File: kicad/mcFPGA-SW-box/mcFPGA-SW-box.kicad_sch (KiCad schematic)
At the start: 120 parts, among them J1 Conn_01x04, J10 Conn_01x02, J11 Conn_01x02, J12 Conn_01x02, J2 Conn_01x04, J4 Conn_01x04, J5 Conn_01x04, J6 Conn_01x04, J8 Conn_01x02, U1 74HC595, U10 NC7SB3157P6X, U11 NC7SB3157P6X, U12 NC7SB3157P6X, U13 NC7SB3157P6X, U14 NC7SB3157P6X, U15 NC7SB3157P6X, U16 NC7SB3157P6X, U17 NC7SB3157P6X, U18 NC7SB3157P6X, U19 NC7SB3157P6X, U2 74HC595, U20 NC7SB3157P6X, U21 NC7SB3157P6X, U22 NC7SB3157P6X, U23 NC7SB3157P6X, U24 NC7SB3157P6X, U25 NC7SB3157P6X, U26 NC7SB3157P6X, U27 NC7SB3157P6X, U28 NC7SB3157P6X, U29 NC7SB3157P6X, U3 74HC595, U30 NC7SB3157P6X, U31 NC7SB3157P6X, U32 NC7SB3157P6X, U33 NC7SB3157P6X, U34 NC7SB3157P6X, U35 NC7SB3157P6X, U36 NC7SB3157P6X, U4 74HC595, U5 NC7SB3157P6X, U6 NC7SB3157P6X, U7 NC7SB3157P6X, U8 NC7SB3157P6X, U9 NC7SB3157P6X

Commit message: start layout of SW box
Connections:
- net GND: now also J1.4 (Pin_4); no longer J1.1 (Pin_1)
- net LATCH: now also J1.3 (Pin_3); no longer J1.2 (Pin_2)
- net MOSI: now also J1.2 (Pin_2); no longer J1.3 (Pin_3)
- net SCLK: now also J1.1 (Pin_1); no longer J1.4 (Pin_4)
- net prio_east_0: no longer J12.2 (Pin_2)
- net prio_west_0: now also U26.1; no longer U26.4
- net prio_west_1: now also U25.1; no longer U25.4
- net west_0: now also U8.3; no longer U8.4
- net west_1: now also U7.3; no longer U7.4
- net west_2: now also U6.3; no longer U6.4
- net west_3: now also U5.3; no longer U5.4
- net at U29.4, U33.4, U36.4: now also U26.4; no longer U26.1
- net at U12.4, U22.4: now also U6.4; no longer U6.1
- net at U28.4, U32.4, U35.4: now also U25.4; no longer U25.1
- net at U18.4, U24.4: now also U8.4; no longer U8.1
- net at U21.4, U9.4: now also U5.4; no longer U5.1
- net at U15.4, U23.4: now also U7.4; no longer U7.1
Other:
- moved on the sheet: J1, J10, J11, J12, J2, J8, U25A, U26A, U27A, U28A, U29A, U30A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

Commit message: SWbox layout nearly complete
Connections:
- net prio_east_0: now also J12.2 (Pin_2)
- net west_0: now also U8.1; no longer U8.3
- net west_1: now also U7.1; no longer U7.3
- net west_2: now also U6.1; no longer U6.3
- net west_3: now also U5.1; no longer U5.3
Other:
- moved on the sheet: J12, J?
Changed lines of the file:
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@@
   (junction (at 158.115 227.965) (diameter 0) (color 0 0 0 0)
   )
+  (no_connect (at 105.41 119.38))
   (no_connect (at 297.18 60.96))
   (no_connect (at 162.56 144.78))
-  (no_connect (at 105.41 106.68))
   (no_connect (at 374.65 60.96))
   (no_connect (at 223.52 109.22))
-  (no_connect (at 105.41 124.46))
   (no_connect (at 142.24 144.78))
-  (no_connect (at 105.41 88.9))
   (no_connect (at 201.93 119.38))
   (no_connect (at 162.56 40.64))
+  (no_connect (at 105.41 66.04))
   (no_connect (at 182.88 40.64))
   (no_connect (at 331.47 116.84))
+  (no_connect (at 105.41 101.6))
   (no_connect (at 182.88 144.78))
   (no_connect (at 331.47 39.37))
@@
   (no_connect (at 161.29 83.82))
   (no_connect (at 351.79 39.37))
-  (no_connect (at 105.41 71.12))
   (no_connect (at 331.47 71.12))
   (no_connect (at 181.61 101.6))
@@
   (no_connect (at 140.97 66.04))
   (no_connect (at 203.2 40.64))
+  (no_connect (at 105.41 83.82))
   (no_connect (at 223.52 73.66))
   (no_connect (at 142.24 40.64))
@@
     (stroke (width 0) (type default))
   )
-  (wire (pts (xy 388.62 68.58) (xy 377.19 68.58))
+  (wire (pts (xy 377.19 68.58) (xy 389.89 68.58))
     (stroke (width 0) (type default))
   )
@@
     (stroke (width 0) (type default))
   )
-  (wire (pts (xy 88.9 88.9) (xy 99.06 88.9))
+  (wire (pts (xy 88.9 93.98) (xy 99.06 93.98))
     (stroke (width 0) (type default))
   )
@@
     (stroke (width 0) (type default))
   )
-  (wire (pts (xy 105.41 83.82) (xy 101.6 83.82))
+  (wire (pts (xy 105.41 88.9) (xy 101.6 88.9))
     (stroke (width 0) (type default))
   )
@@
     (stroke (width 0) (type default))
   )
-  (wire (pts (xy 88.9 96.52) (xy 99.06 96.52))
+  (wire (pts (xy 88.9 101.6) (xy 99.06 101.6))
     (stroke (width 0) (type default))
   )
@@
     (stroke (width 0) (type default))
   )
-  (wire (pts (xy 101.6 83.82) (xy 101.6 91.44))
+  (wire (pts (xy 101.6 88.9) (xy 101.6 96.52))
     (stroke (width 0) (type default))
   )
@@
     (stroke (width 0) (type default))
   )
-  (wire (pts (xy 88.9 93.98) (xy 101.6 93.98))
+  (wire (pts (xy 88.9 99.06) (xy 101.6 99.06))
     (stroke (width 0) (type default))
   )
@@
     (stroke (width 0) (type default))
   )
-  (wire (pts (xy 374.65 66.04) (xy 389.255 66.04))
+  (wire (pts (xy 374.65 66.04) (xy 389.89 66.04))
     (stroke (width 0) (type default))
   )
@@
     (stroke (width 0) (type default))
   )
-  (wire (pts (xy 105.41 119.38) (xy 99.06 119.38))
+  (wire (pts (xy 105.41 124.46) (xy 99.06 124.46))
     (stroke (width 0) (type default))
   )
@@
     (stroke (width 0) (type default))
   )
-  (wire (pts (xy 99.06 66.04) (xy 99.06 88.9))
+  (wire (pts (xy 99.06 71.12) (xy 99.06 93.98))
     (stroke (width 0) (type default))
   )
@@
     (stroke (width 0) (type default))
   )
-  (wire (pts (xy 105.41 66.04) (xy 99.06 66.04))
+  (wire (pts (xy 105.41 71.12) (xy 99.06 71.12))
     (stroke (width 0) (type default))
   )
@@
     (stroke (width 0) (type default))
   )
-  (wire (pts (xy 105.41 101.6) (xy 101.6 101.6))
+  (wire (pts (xy 105.41 106.68) (xy 101.6 106.68))
     (stroke (width 0) (type default))
   )
@@
     (stroke (width 0) (type default))
   )
-  (wire (pts (xy 101.6 101.6) (xy 101.6 93.98))
+  (wire (pts (xy 101.6 106.68) (xy 101.6 99.06))
     (stroke (width 0) (type default))
   )
@@
     (stroke (width 0) (type default))
   )
-  (wire (pts (xy 88.9 91.44) (xy 101.6 91.44))
-    (stroke (width 0) (type default))
-  )
-  (wire (pts (xy 99.06 119.38) (xy 99.06 96.52))
+  (wire (pts (xy 88.9 96.52) (xy 101.6 96.52))
+    (stroke (width 0) (type default))
+  )
+  (wire (pts (xy 99.06 124.46) (xy 99.06 101.6))
     (stroke (width 0) (type default))
   )
@@
     (effects (font (size 1.27 1.27)) (justify left bottom))
   )
-  (label "west_1" (at 90.17 93.98 0) (fields_autoplaced)
+  (label "west_1" (at 90.17 99.06 0) (fields_autoplaced)
     (effects (font (size 1.27 1.27)) (justify left bottom))
   )
@@
     (effects (font (size 1.27 1.27)) (justify left bottom))
   )
-  (label "west_3" (at 90.17 88.9 0) (fields_autoplaced)
+  (label "west_3" (at 90.17 93.98 0) (fields_autoplaced)
     (effects (font (size 1.27 1.27)) (justify left bottom))
   )
@@
     (effects (font (size 1.27 1.27)) (justify left bottom))
   )
-  (label "west_2" (at 90.17 91.44 0) (fields_autoplaced)
+  (label "west_2" (at 90.17 96.52 0) (fields_autoplaced)
     (effects (font (size 1.27 1.27)) (justify left bottom))
   )
@@
     (effects (font (size 1.27 1.27)) (justify left bottom))
   )
-  (label "west_0" (at 90.17 96.52 0) (fields_autoplaced)
+  (label "west_0" (at 90.17 101.6 0) (fields_autoplaced)
     (effects (font (size 1.27 1.27)) (justify left bottom))
   )
@@
     )
   )
-  (symbol (lib_id "Connector_Generic:Conn_01x04") (at 83.82 93.98 180) (unit 1)
+  (symbol (lib_id "Connector_Generic:Conn_01x04") (at 83.82 99.06 180) (unit 1)
     (in_bom yes) (on_board yes) (dnp no)
-    (property "Reference" "J?" (at 85.09 100.33 0)
+    (property "Reference" "J?" (at 85.09 105.41 0)
       (effects (font (size 1.27 1.27)) (justify left))
     )
-    (property "Value" "Conn_01x04" (at 80.01 88.9 0)
+    (property "Value" "Conn_01x04" (at 80.01 93.98 0)
       (effects (font (size 1.27 1.27)) (justify left))
     )
-    (property "Footprint" "Connector_PinHeader_2.54mm:PinHeader_1x04_P2.54mm_Horizontal" (at 83.82 93.98 0)
-      (effects (font (size 1.27 1.27)) hide)
-    )
-    (property "Datasheet" "~" (at 83.82 93.98 0)
-      (effects (font (size 1.27 1.27)) hide)
-    )
-    (property "JLCPCB Part #" "do not place" (at 83.82 93.98 0)
-      (effects (font (size 1.27 1.27)) hide)
-    )
-    (property "Part Nr." "do not place" (at 83.82 93.98 0)
-      (effects (font (size 1.27 1.27)) hide)
-    )
-    (property "Dielectric" "" (at 83.82 93.98 0)
-      (effects (font (size 1.27 1.27)) hide)
-    )
-    (property "Voltage" "" (at 83.82 93.98 0)
-      (effects (font (size 1.27 1.27)) hide)
-    )
-    (property "JLCPCB Alt #" "do not place" (at 83.82 93.98 0)
-      (effects (font (size 1.27 1.27)) hide)
-    )
-    (property "package" "" (at 83.82 93.98 0)
+    (property "Footprint" "Connector_PinHeader_2.54mm:PinHeader_1x04_P2.54mm_Horizontal" (at 83.82 99.06 0)
+      (effects (font (size 1.27 1.27)) hide)
+    )
+    (property "Datasheet" "~" (at 83.82 99.06 0)
+      (effects (font (size 1.27 1.27)) hide)
+    )
+    (property "JLCPCB Part #" "do not place" (at 83.82 99.06 0)
+      (effects (font (size 1.27 1.27)) hide)
+    )
+    (property "Part Nr." "do not place" (at 83.82 99.06 0)
+      (effects (font (size 1.27 1.27)) hide)
+    )
+    (property "Dielectric" "" (at 83.82 99.06 0)
+      (effects (font (size 1.27 1.27)) hide)
+    )
+    (property "Voltage" "" (at 83.82 99.06 0)
+      (effects (font (size 1.27 1.27)) hide)
+    )
+    (property "JLCPCB Alt #" "do not place" (at 83.82 99.06 0)
+      (effects (font (size 1.27 1.27)) hide)
+    )
+    (property "package" "" (at 83.82 99.06 0)
       (effects (font (size 1.27 1.27)) hide)
     )
@@
     )
   )
-  (symbol (lib_id "Connector_Generic:Conn_01x02") (at 394.335 66.04 0) (unit 1)
+  (symbol (lib_id "Connector_Generic:Conn_01x02") (at 394.97 66.04 0) (unit 1)
     (in_bom yes) (on_board yes) (dnp no)
-    (property "Reference" "J12" (at 396.875 69.215 0)
+    (property "Reference" "J12" (at 397.51 69.215 0)
       (effects (font (size 1.27 1.27)) (justify left))
     )
-    (property "Value" "Conn_01x02" (at 396.875 66.04 0)
+    (property "Value" "Conn_01x02" (at 397.51 66.04 0)
       (effects (font (size 1.27 1.27)) (justify left))
     )
-    (property "Footprint" "Connector_PinHeader_2.54mm:PinHeader_1x02_P2.54mm_Horizontal" (at 394.335 66.04 0)
-      (effects (font (size 1.27 1.27)) hide)
-    )
-    (property "Datasheet" "~" (at 394.335 66.04 0)
-      (effects (font (size 1.27 1.27)) hide)
-    )
+    (property "Footprint" "Connector_PinHeader_2.54mm:PinHeader_1x02_P2.54mm_Horizontal" (at 394.97 66.04 0)
+      (effects (font (size 1.27 1.27)) hide)
+    )
+    (property "Datasheet" "~" (at 394.97 66.04 0)
+      (effects (font (size 1.27 1.27)) hide)
+    )

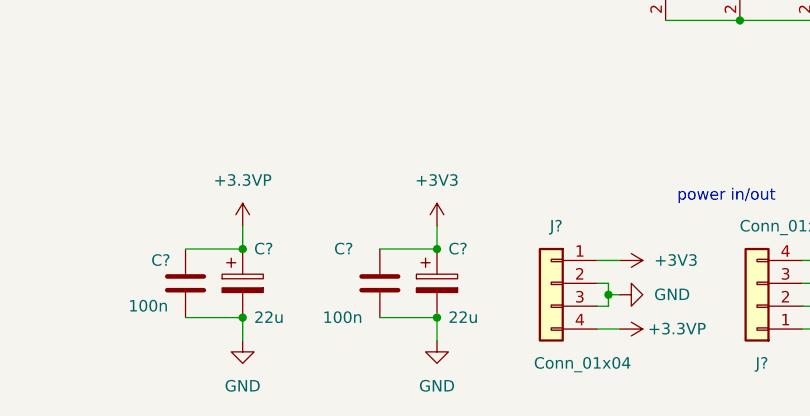
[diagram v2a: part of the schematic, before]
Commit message: sw box layout almost complete
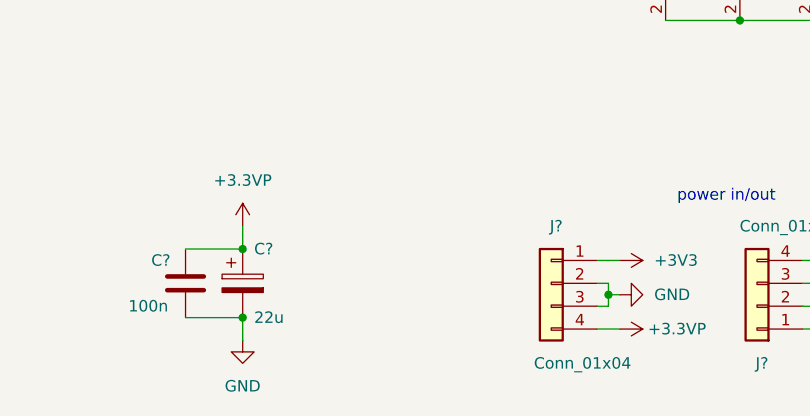
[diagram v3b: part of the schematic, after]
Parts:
- removed C?: 22u, Resistor_SMD:R_1206_3216Metric, symbol Device:C_Polarized
- removed C?: 100n, Capacitor_SMD:C_0603_1608Metric, symbol Device:C
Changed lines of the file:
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@@
   (junction (at 128.27 269.875) (diameter 0) (color 0 0 0 0)
   )
-  (junction (at 242.57 274.32) (diameter 0) (color 0 0 0 0)
-  )
   (junction (at 347.345 215.9) (diameter 0) (color 0 0 0 0)
   )
@@
   (junction (at 314.96 63.5) (diameter 0) (color 0 0 0 0)
   )
-  (junction (at 242.57 266.7) (diameter 0) (color 0 0 0 0)
-  )
   (junction (at 380.365 241.3) (diameter 0) (color 0 0 0 0)
   )
@@
     (stroke (width 0) (type default))
   )
-  (wire (pts (xy 236.22 274.32) (xy 242.57 274.32))
-    (stroke (width 0) (type default))
-  )
   (wire (pts (xy 102.87 224.155) (xy 102.87 227.965))
     (stroke (width 0) (type default))
@@
     (stroke (width 0) (type default))
   )
-  (wire (pts (xy 236.22 266.7) (xy 242.57 266.7))
-    (stroke (width 0) (type default))
-  )
   (wire (pts (xy 173.99 156.21) (xy 175.26 156.21))
     (stroke (width 0) (type default))
@@
     (stroke (width 0) (type default))
   )
-  (wire (pts (xy 242.57 264.16) (xy 242.57 266.7))
-    (stroke (width 0) (type default))
-  )
   (wire (pts (xy 153.035 202.565) (xy 153.035 208.915))
     (stroke (width 0) (type default))
@@
     (stroke (width 0) (type default))
   )
-  (wire (pts (xy 242.57 274.32) (xy 242.57 276.86))
-    (stroke (width 0) (type default))
-  )
   (wire (pts (xy 172.72 113.03) (xy 173.99 113.03))
     (stroke (width 0) (type default))
@@
     )
   )
-  (symbol (lib_id "power:+3V3") (at 242.57 264.16 0) (unit 1)
-    (in_bom yes) (on_board yes) (dnp no) (fields_autoplaced)
-    (property "Reference" "#PWR?" (at 242.57 267.97 0)
-      (effects (font (size 1.27 1.27)) hide)
-    )
-    (property "Value" "+3V3" (at 242.57 259.08 0)
-      (effects (font (size 1.27 1.27)))
-    )
-    (property "Footprint" "" (at 242.57 264.16 0)
-      (effects (font (size 1.27 1.27)) hide)
-    )
-    (property "Datasheet" "" (at 242.57 264.16 0)
-      (effects (font (size 1.27 1.27)) hide)
-    )
-    (pin "1")
-    (instances
-      (project "myFPGA-CLB-slice"
-        (path "/2d29d97f-956a-4594-9321-3d88807a498d/4edb728f-4165-4dad-bea7-d5caa521ea2d"
-          (reference "#PWR?") (unit 1)
-        )
-        (path "/2d29d97f-956a-4594-9321-3d88807a498d/2ae8c962-eb3a-4bc0-879b-9a9a0cb7ca8b"
-          (reference "#PWR?") (unit 1)
-        )
-        (path "/2d29d97f-956a-4594-9321-3d88807a498d/c0683758-8f95-4956-98b3-1cadd07503a7"
-          (reference "#PWR?") (unit 1)
-        )
-        (path "/2d29d97f-956a-4594-9321-3d88807a498d/8d6c6a11-91f4-4cda-a0a3-b01338b326ab"
-          (reference "#PWR?") (unit 1)
-        )
-        (path "/2d29d97f-956a-4594-9321-3d88807a498d/f8f5aa5a-daee-44c0-974a-67be9fa42cb8"
-          (reference "#PWR?") (unit 1)
-        )
-        (path "/2d29d97f-956a-4594-9321-3d88807a498d"
-          (reference "#PWR?") (unit 1)
-        )
-      )
-      (project "mcFPGA-SW-box"
-        (path "/75464c66-5d03-4301-9167-50ec2376d3e1"
-          (reference "#PWR033") (unit 1)
-        )
-      )
-      (project "myFPGA-CBv"
-        (path "/e7dd8cdd-7178-4795-89bd-2ea837b9d4c9"
-          (reference "#PWR?") (unit 1)
-        )
-      )
-    )
-  )
   (symbol (lib_id "Connector_Generic:Conn_01x02") (at 394.97 66.04 0) (unit 1)
     (in_bom yes) (on_board yes) (dnp no)
@@
     )
   )
-  (symbol (lib_id "Device:C_Polarized") (at 242.57 270.51 0) (unit 1)
-    (in_bom yes) (on_board yes) (dnp no)
-    (property "Reference" "C?" (at 243.84 266.7 0)
-      (effects (font (size 1.27 1.27)) (justify left))
-    )
-    (property "Value" "22u" (at 243.84 274.32 0)
-      (effects (font (size 1.27 1.27)) (justify left))
-    )
-    (property "Footprint" "Resistor_SMD:R_1206_3216Metric" (at 243.5352 274.32 0)
-      (effects (font (size 1.27 1.27)) hide)
-    )
-    (property "Datasheet" "~" (at 242.57 270.51 0)
-      (effects (font (size 1.27 1.27)) hide)
-    )
-    (property "Dielectric" "X5R" (at 242.57 270.51 0)
-      (effects (font (size 1.27 1.27)) hide)
-    )
-    (property "JLCPCB Part #" "C12891" (at 242.57 270.51 0)
-      (effects (font (size 1.27 1.27)) hide)
-    )
-    (property "Part Nr." "CL31A226KAHNNNE" (at 242.57 270.51 0)
-      (effects (font (size 1.27 1.27)) hide)
-    )
-    (property "Voltage" "25" (at 242.57 270.51 0)
-      (effects (font (size 1.27 1.27)) hide)
-    )
-    (property "JLCPCB Alt #" "" (at 242.57 270.51 0)
-      (effects (font (size 1.27 1.27)) hide)
-    )
-    (property "package" "" (at 242.57 270.51 0)
-      (effects (font (size 1.27 1.27)) hide)
-    )
-    (pin "1")
-    (pin "2")
-    (instances
-      (project "myFPGA-CLB-slice"
-        (path "/2d29d97f-956a-4594-9321-3d88807a498d"
-          (reference "C?") (unit 1)
-        )
-      )
-      (project "mcFPGA-SW-box"
-        (path "/75464c66-5d03-4301-9167-50ec2376d3e1"
-          (reference "C8") (unit 1)
-        )
-      )
-      (project "myFPGA-CBv"
-        (path "/e7dd8cdd-7178-4795-89bd-2ea837b9d4c9"
-          (reference "C?") (unit 1)
-        )
-      )
-    )
-  )
   (symbol (lib_id "Device:R") (at 158.115 254.635 0) (unit 1)
     (in_bom yes) (on_board yes) (dnp no)
@@
         )
       )
-    )
-  )
-  (symbol (lib_id "power:GND") (at 242.57 276.86 0) (unit 1)
-    (in_bom yes) (on_board yes) (dnp no) (fields_autoplaced)
-    (property "Reference" "#PWR?" (at 242.57 283.21 0)
-      (effects (font (size 1.27 1.27)) hide)
-    )
-    (property "Value" "GND" (at 242.57 281.94 0)
-      (effects (font (size 1.27 1.27)))
-    )
-    (property "Footprint" "" (at 242.57 276.86 0)
-      (effects (font (size 1.27 1.27)) hide)
-    )
-    (property "Datasheet" "" (at 242.57 276.86 0)
-      (effects (font (size 1.27 1.27)) hide)
-    )
-    (pin "1")
-    (instances
-      (project "myFPGA-CLB-slice"
-        (path "/2d29d97f-956a-4594-9321-3d88807a498d/4edb728f-4165-4dad-bea7-d5caa521ea2d"
-          (reference "#PWR?") (unit 1)
-        )
-        (path "/2d29d97f-956a-4594-9321-3d88807a498d/2ae8c962-eb3a-4bc0-879b-9a9a0cb7ca8b"
-          (reference "#PWR?") (unit 1)
-        )
-        (path "/2d29d97f-956a-4594-9321-3d88807a498d/c0683758-8f95-4956-98b3-1cadd07503a7"
-          (reference "#PWR?") (unit 1)
-        )
-        (path "/2d29d97f-956a-4594-9321-3d88807a498d/8d6c6a11-91f4-4cda-a0a3-b01338b326ab"
-          (reference "#PWR?") (unit 1)
-        )
-        (path "/2d29d97f-956a-4594-9321-3d88807a498d/f8f5aa5a-daee-44c0-974a-67be9fa42cb8"
-          (reference "#PWR?") (unit 1)
-        )
-        (path "/2d29d97f-956a-4594-9321-3d88807a498d"
-          (reference "#PWR?") (unit 1)
-        )
-      )
-      (project "mcFPGA-SW-box"
-        (path "/75464c66-5d03-4301-9167-50ec2376d3e1"
-          (reference "#PWR034") (unit 1)
-        )
-      )
-      (project "myFPGA-CBv"
-        (path "/e7dd8cdd-7178-4795-89bd-2ea837b9d4c9"
-          (reference "#PWR?") (unit 1)
-        )
-      )
-    )
-  )
-  (symbol (lib_id "Device:C") (at 236.22 270.51 0) (unit 1)
-    (in_bom yes) (on_board yes) (dnp no)
-    (property "Reference" "C?" (at 231.14 266.7 0)
-      (effects (font (size 1.27 1.27)) (justify left))
-    )
-    (property "Value" "100n" (at 229.87 274.32 0)
-      (effects (font (size 1.27 1.27)) (justify left))
-    )
-    (property "Footprint" "Capacitor_SMD:C_0603_1608Metric" (at 237.1852 274.32 0)
-      (effects (font (size 1.27 1.27)) hide)
-    )
-    (property "Datasheet" "~" (at 236.22 270.51 0)
-      (effects (font (size 1.27 1.27)) hide)
-    )
-    (property "JLCPCB Part #" "C14663" (at 236.22 270.51 0)
-      (effects (font (size 1.27 1.27)) hide)
-    )
-    (property "Part Nr." "CC0603KRX7R9BB104" (at 236.22 270.51 0)
-      (effects (font (size 1.27 1.27)) hide)
-    )
-    (property "Dielectric" "X7R" (at 236.22 270.51 0)
-      (effects (font (size 1.27 1.27)) hide)
-    )
-    (property "Voltage" "50" (at 236.22 270.51 0)
-      (effects (font (size 1.27 1.27)) hide)
-    )
-    (property "JLCPCB Alt #" "" (at 236.22 270.51 0)
-      (effects (font (size 1.27 1.27)) hide)
-    )
-    (property "package" "" (at 236.22 270.51 0)
-      (effects (font (size 1.27 1.27)) hide)
-    )
-    (pin "1")
-    (pin "2")
-    (instances
-      (project "myFPGA-CLB-slice"
-        (path "/2d29d97f-956a-4594-9321-3d88807a498d/4edb728f-4165-4dad-bea7-d5caa521ea2d"
-          (reference "C?") (unit 1)
-        )
-        (path "/2d29d97f-956a-4594-9321-3d88807a498d/2ae8c962-eb3a-4bc0-879b-9a9a0cb7ca8b"
-          (reference "C?") (unit 1)
-        )
-        (path "/2d29d97f-956a-4594-9321-3d88807a498d/c0683758-8f95-4956-98b3-1cadd07503a7"
-          (reference "C?") (unit 1)
-        )
-        (path "/2d29d97f-956a-4594-9321-3d88807a498d/8d6c6a11-91f4-4cda-a0a3-b01338b326ab"
-          (reference "C?") (unit 1)
-        )
-        (path "/2d29d97f-956a-4594-9321-3d88807a498d/f8f5aa5a-daee-44c0-974a-67be9fa42cb8"
-          (reference "C?") (unit 1)
-        )
-        (path "/2d29d97f-956a-4594-9321-3d88807a498d"
-          (reference "C?") (unit 1)
-        )
-      )
-      (project "mcFPGA-SW-box"
-        (path "/75464c66-5d03-4301-9167-50ec2376d3e1"
-          (reference "C7") (unit 1)
-        )
-      )
-      (project "myFPGA-CBv"
-        (path "/e7dd8cdd-7178-4795-89bd-2ea837b9d4c9"
-          (reference "C?") (unit 1)
-        )
-      )
